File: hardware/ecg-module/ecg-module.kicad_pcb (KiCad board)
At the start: 2 copper layers, 58 x 58 mm, 45 parts, among them IC1 AP2112K-1.8TRG1, J1 ST_01x02, J2 LEFT-UI, J3 RIGHT-UI

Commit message: Add silkscreen texts
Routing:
- net Net-(J1-Pad2): track 42.3 -> 43.5 mm
- net Net-(J1-Pad1): track 46.5 -> 47.2 mm
- added copper zone on F.Cu, net GND
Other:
- board text added: "1V8"
- board text added: "3V3"
- board text added: "5V"
- board text added: "CSB"
- board text added: "E+"
- board text added: "E-"
- board text added: "ECGN"
- board text added: "ECGP"
- board text added: "GND"
- board text added: "GNDA"
- board text added: "INT2B"
- board text added: "INTB"
- board text added: "MISO"
- board text added: "MOSI"
- board text added: "SCLK"
- board text added: "araBeat ECG Module v0.1 Designed by Aravinth www.aravinth.info"

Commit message: Add ecg heart logo
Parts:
- added G***: LOGO, ECG-MODULE:ecg-heart, F.Cu at (136.6, 117.1)
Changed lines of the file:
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@@
     (tracks 584)
     (zones 0)
-    (modules 45)
+    (modules 46)
     (nets 31)
   )
@@
     (34 B.Paste user)
     (35 F.Paste user)
-    (36 B.SilkS user)
+    (36 B.SilkS user hide)
     (37 F.SilkS user)
     (38 B.Mask user hide)
@@
     (pad_drill 0.6)
     (pad_to_mask_clearance 0)
-    (aux_axis_origin 123.571 80.0862)
+    (aux_axis_origin 123.571 130.0988)
     (visible_elements FFFFFF7F)
     (pcbplotparams
@@
     )
   )
+  (module ECG-MODULE:ecg-heart (layer F.Cu)
+    (at 136.571 117.0988)
+    (fp_text reference G*** (at 0 0) (layer F.SilkS) hide
+      (effects (font (size 1.524 1.524) (thickness 0.3)))
+    )
+    (fp_text value LOGO (at 0.75 0) (layer F.SilkS) hide
+      (effects (font (size 1.524 1.524) (thickness 0.3)))
+    )
+    (fp_poly (pts (xy 2.280248 -3.43974) (xy 2.852631 -3.27243) (xy 3.319209 -2.977796) (xy 3.669441 -2.56851)
+      (xy 3.892785 -2.057244) (xy 3.978701 -1.456671) (xy 3.979333 -1.397244) (xy 3.966477 -0.983557)
+      (xy 3.931633 -0.658812) (xy 3.880389 -0.439395) (xy 3.81833 -0.341692) (xy 3.751044 -0.382086)
+      (xy 3.690565 -0.550333) (xy 3.62179 -0.72313) (xy 3.532287 -0.736612) (xy 3.407363 -0.590148)
+      (xy 3.373856 -0.536711) (xy 3.262115 -0.395852) (xy 3.11122 -0.327178) (xy 2.859743 -0.304629)
+      (xy 2.825079 -0.303877) (xy 2.413 -0.296333) (xy 2.282773 0.229005) (xy 2.206213 0.511003)
+      (xy 2.136062 0.724031) (xy 2.092273 0.814616) (xy 2.073106 0.754249) (xy 2.056455 0.54987)
+      (xy 2.04336 0.226793) (xy 2.034864 -0.189665) (xy 2.032 -0.650448) (xy 2.028759 -1.199605)
+      (xy 2.019796 -1.743741) (xy 2.006248 -2.238311) (xy 1.989254 -2.638766) (xy 1.976145 -2.836542)
+      (xy 1.920291 -3.4973) (xy 2.280248 -3.43974)) (layer F.SilkS) (width 0.01))
+    (fp_poly (pts (xy -2.936109 -1.382913) (xy -2.91381 -1.212006) (xy -2.897222 -0.896742) (xy -2.88713 -0.449586)
+      (xy -2.884618 -0.148167) (xy -2.884391 0.320475) (xy -2.887516 0.723793) (xy -2.893507 1.034094)
+      (xy -2.901879 1.223683) (xy -2.909485 1.27) (xy -2.970089 1.206192) (xy -3.087539 1.044962)
+      (xy -3.149926 0.9525) (xy -3.397539 0.5713) (xy -3.553744 0.307574) (xy -3.624074 0.139955)
+      (xy -3.614059 0.047078) (xy -3.529233 0.007576) (xy -3.396542 0) (xy -3.234903 -0.026824)
+      (xy -3.13114 -0.126442) (xy -3.072635 -0.327576) (xy -3.046771 -0.658946) (xy -3.043205 -0.804333)
+      (xy -3.024688 -1.088878) (xy -2.98592 -1.324882) (xy -2.963333 -1.397) (xy -2.936109 -1.382913)) (layer F.SilkS) (width 0.01))
+    (fp_poly (pts (xy 1.576632 -2.565757) (xy 1.53493 -1.893824) (xy 1.499893 -1.372098) (xy 1.46887 -0.981707)
+      (xy 1.439212 -0.70378) (xy 1.408269 -0.519448) (xy 1.37339 -0.409839) (xy 1.331925 -0.356083)
+      (xy 1.281225 -0.339309) (xy 1.263868 -0.338667) (xy 1.098837 -0.274202) (xy 0.990368 -0.167485)
+      (xy 0.889647 -0.053184) (xy 0.807975 -0.076169) (xy 0.763534 -0.125152) (xy 0.668661 -0.188631)
+      (xy 0.491313 -0.22851) (xy 0.201552 -0.248904) (xy -0.173995 -0.254) (xy -0.563667 -0.254338)
+      (xy -0.81777 -0.270597) (xy -0.969925 -0.325649) (xy -1.053755 -0.442363) (xy -1.10288 -0.643611)
+      (xy -1.144989 -0.914498) (xy -1.205901 -1.158933) (xy -1.286145 -1.235315) (xy -1.385407 -1.143781)
+      (xy -1.503373 -0.88447) (xy -1.555142 -0.735577) (xy -1.648166 -0.468346) (xy -1.728067 -0.324454)
+      (xy -1.832637 -0.265744) (xy -1.999669 -0.254056) (xy -2.032101 -0.254) (xy -2.237363 -0.231339)
+      (xy -2.363917 -0.142629) (xy -2.429761 0.043216) (xy -2.452894 0.357284) (xy -2.454177 0.475016)
+      (xy -2.467539 0.818684) (xy -2.500935 1.144261) (xy -2.547707 1.410275) (xy -2.601196 1.575254)
+      (xy -2.636175 1.608667) (xy -2.657353 1.528008) (xy -2.676209 1.30205) (xy -2.691797 0.954824)
+      (xy -2.703173 0.510359) (xy -2.70939 -0.007316) (xy -2.710265 -0.275167) (xy -2.713703 -1.039473)
+      (xy -2.723783 -1.647388) (xy -2.741413 -2.111757) (xy -2.767499 -2.445425) (xy -2.802949 -2.661236)
+      (xy -2.84867 -2.772035) (xy -2.888132 -2.794) (xy -2.938917 -2.766738) (xy -2.983077 -2.671008)
+      (xy -3.024419 -2.485889) (xy -3.066749 -2.190465) (xy -3.113872 -1.763817) (xy -3.157733 -1.312333)
+      (xy -3.201817 -0.862213) (xy -3.239271 -0.553448) (xy -3.27703 -0.358603) (xy -3.32203 -0.250244)
+      (xy -3.381207 -0.200937) (xy -3.44257 -0.185693) (xy -3.564557 -0.195566) (xy -3.635791 -0.297275)
+      (xy -3.682188 -0.503193) (xy -3.750013 -0.740817) (xy -3.843516 -0.844531) (xy -3.859776 -0.846667)
+      (xy -3.92776 -0.923034) (xy -3.968736 -1.122913) (xy -3.981559 -1.402469) (xy -3.965086 -1.717868)
+      (xy -3.918172 -2.025274) (xy -3.893192 -2.127053) (xy -3.71058 -2.517409) (xy -3.409322 -2.884825)
+      (xy -3.038076 -3.180214) (xy -2.688133 -3.342786) (xy -2.031984 -3.452056) (xy -1.362775 -3.404953)
+      (xy -0.717714 -3.206801) (xy -0.340339 -3.006723) (xy -0.029322 -2.810386) (xy 0.556839 -3.092002)
+      (xy 0.876832 -3.237402) (xy 1.169807 -3.356207) (xy 1.376248 -3.424415) (xy 1.387695 -3.427066)
+      (xy 1.63239 -3.480514) (xy 1.576632 -2.565757)) (layer F.SilkS) (width 0.01))
+    (fp_poly (pts (xy 1.794442 -2.51084) (xy 1.817297 -2.291671) (xy 1.838109 -1.937108) (xy 1.856007 -1.464122)
+      (xy 1.87012 -0.889681) (xy 1.876248 -0.515266) (xy 1.886775 0.066967) (xy 1.901237 0.593105)
+      (xy 1.918579 1.039457) (xy 1.93775 1.382331) (xy 1.957695 1.598037) (xy 1.973103 1.662758)
+      (xy 2.059388 1.674022) (xy 2.145037 1.529689) (xy 2.232481 1.224422) (xy 2.28287 0.982599)
+      (xy 2.371508 0.525475) (xy 2.442398 0.208792) (xy 2.510153 0.006778) (xy 2.589389 -0.106339)
+      (xy 2.694719 -0.156331) (xy 2.840758 -0.168969) (xy 2.936096 -0.169333) (xy 3.241178 -0.19948)
+      (xy 3.41632 -0.29572) (xy 3.433389 -0.316654) (xy 3.516095 -0.405101) (xy 3.579782 -0.365685)
+      (xy 3.644388 -0.237311) (xy 3.694298 -0.086283) (xy 3.679199 0.061343) (xy 3.586985 0.263448)
+      (xy 3.511756 0.396843) (xy 3.004062 1.148299) (xy 2.387039 1.856602) (xy 1.699758 2.482763)
+      (xy 0.98129 2.987796) (xy 0.825694 3.077248) (xy 0.466422 3.268565) (xy 0.209525 3.380045)
+      (xy 0.012755 3.419927) (xy -0.166136 3.396451) (xy -0.369397 3.31786) (xy -0.381 3.312612)
+      (xy -0.835675 3.073071) (xy -1.333763 2.757474) (xy -1.803035 2.413466) (xy -2.021461 2.230503)
+      (xy -2.391921 1.900731) (xy -2.243667 -0.042333) (xy -1.911618 -0.084667) (xy -1.682335 -0.135107)
+      (xy -1.560892 -0.238614) (xy -1.502744 -0.381) (xy -1.415577 -0.653426) (xy -1.356352 -0.770535)
+      (xy -1.308387 -0.740355) (xy -1.255002 -0.570918) (xy -1.238919 -0.508) (xy -1.143 -0.127)
+      (xy -0.237645 -0.103018) (xy 0.167237 -0.08944) (xy 0.434079 -0.070219) (xy 0.594173 -0.039132)
+      (xy 0.678809 0.01004) (xy 0.71928 0.083518) (xy 0.72056 0.087482) (xy 0.818189 0.232091)
+      (xy 0.947221 0.224345) (xy 1.073258 0.06792) (xy 1.082292 0.048849) (xy 1.222484 -0.117129)
+      (xy 1.371049 -0.183985) (xy 1.478816 -0.216891) (xy 1.545456 -0.304003) (xy 1.58801 -0.484898)
+      (xy 1.619937 -0.762) (xy 1.650312 -1.153905) (xy 1.673815 -1.602488) (xy 1.683437 -1.92117)
+      (xy 1.698287 -2.226217) (xy 1.728133 -2.459666) (xy 1.766773 -2.57473) (xy 1.770415 -2.577646)
+      (xy 1.794442 -2.51084)) (layer F.SilkS) (width 0.01))
+  )
   (gr_text MISO (at 170.688 111.633 90) (layer F.SilkS)

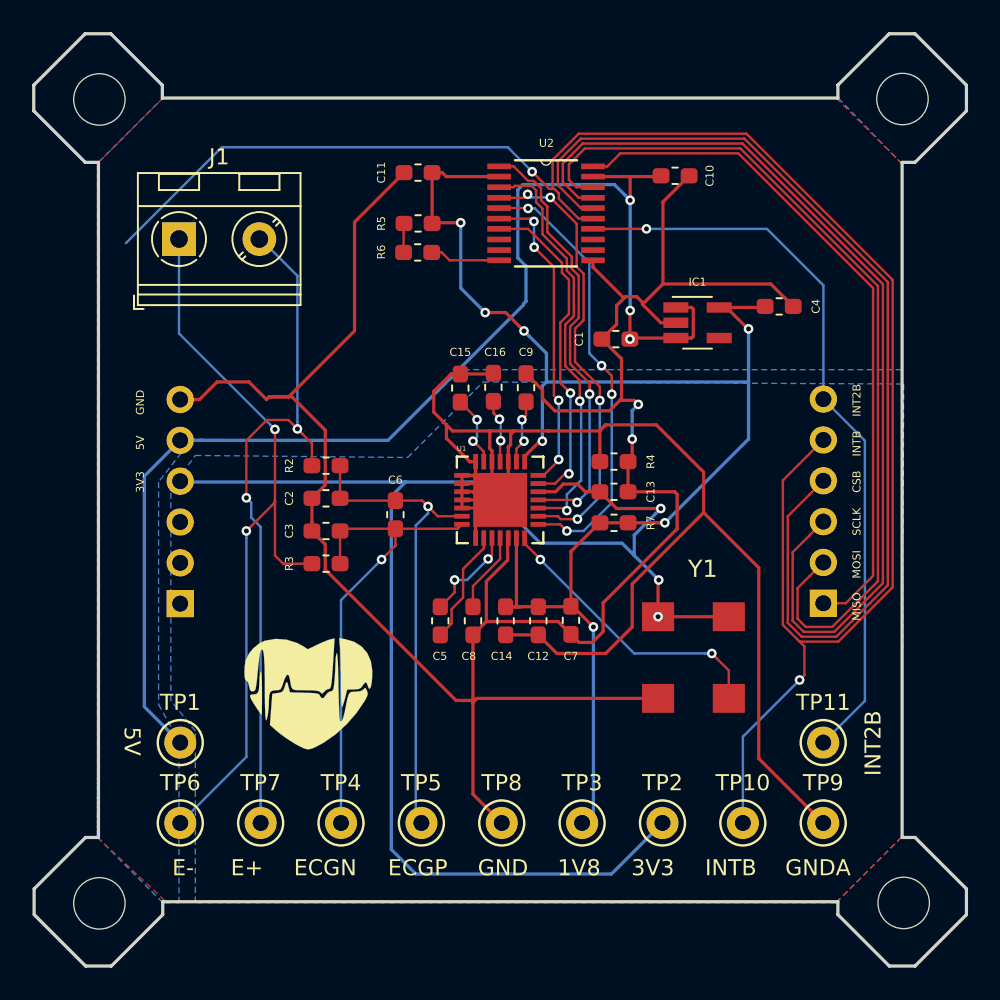
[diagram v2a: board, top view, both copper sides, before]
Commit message: Clean up traces, add design label on copper
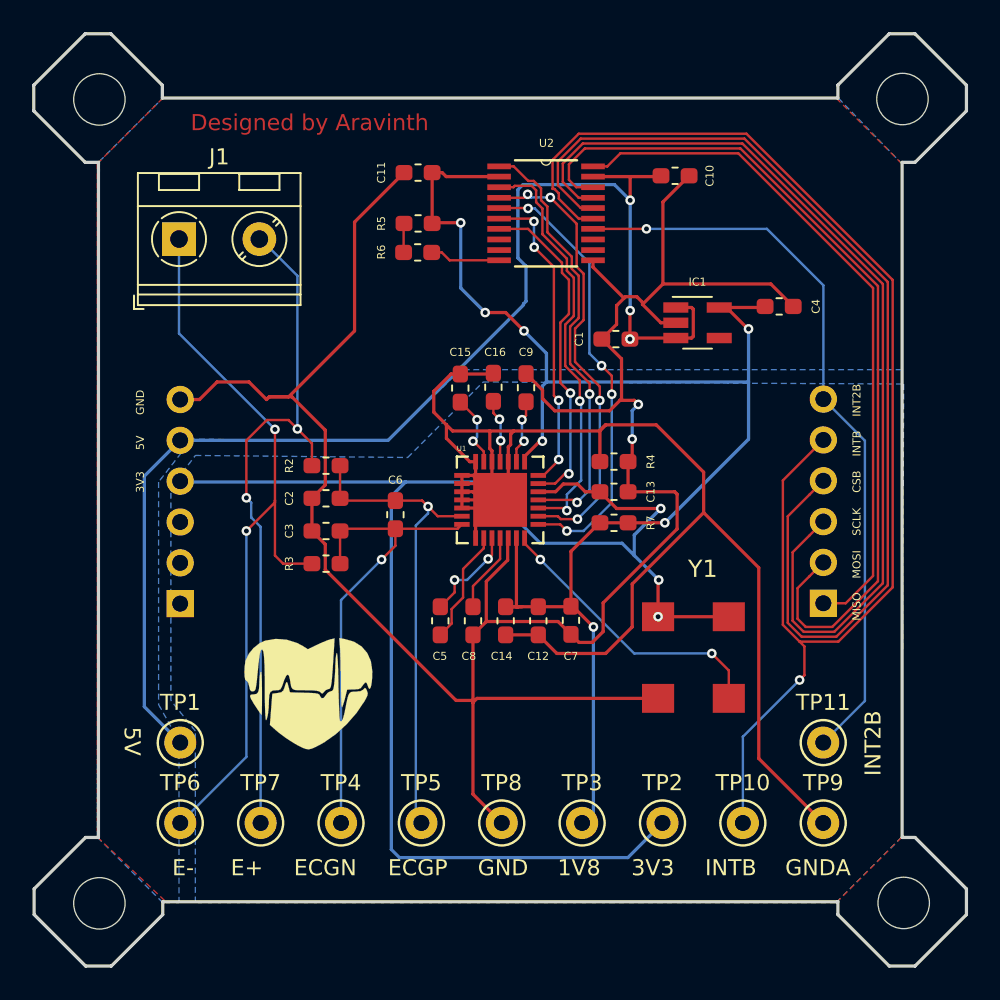
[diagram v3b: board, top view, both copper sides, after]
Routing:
- net INTB_5V: track 114.3 -> 84.2 mm, vias 2 -> 1
- net +3V3: track 93.3 -> 92.5 mm
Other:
- board text added: "Designed by Aravinth"
- board text added: "araBeat ECG Module v0.1 www.aravinth.info"
- board text removed: "araBeat ECG Module v0.1 Designed by Aravinth www.aravinth.info"
